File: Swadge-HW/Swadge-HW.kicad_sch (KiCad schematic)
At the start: 178 parts, among them J1 Conn_02x03_Odd_Even, J2 PJ-307C, J3 Conn_01x05_Male, P1 USB_C_Plug_USB2.0, Q1 Q_PMOS_GSD, SW1 YTS-D003-1A, SW2 YTS-D003-1A, SW3 YTS-D003-1A, SW4 YTS-D003-1A, SW5 YTS-D003-1A, SW6 YTS-D003-1A, SW7 B3FS-4002P, SW8 B3FS-4002P, SW9 SW_SPDT_1825232-1, U1 ESP32-S2-MINI-1, U11 CH32V003F4U6, U2 RB017A1505A, U3 M3410, U5 RB017A1505A_Connector, U6 LSM6DSL, U7 GENERIC_LDO_GOI, U8 FM8002A, U9 INGHAi_GSPK2307P-8R1W

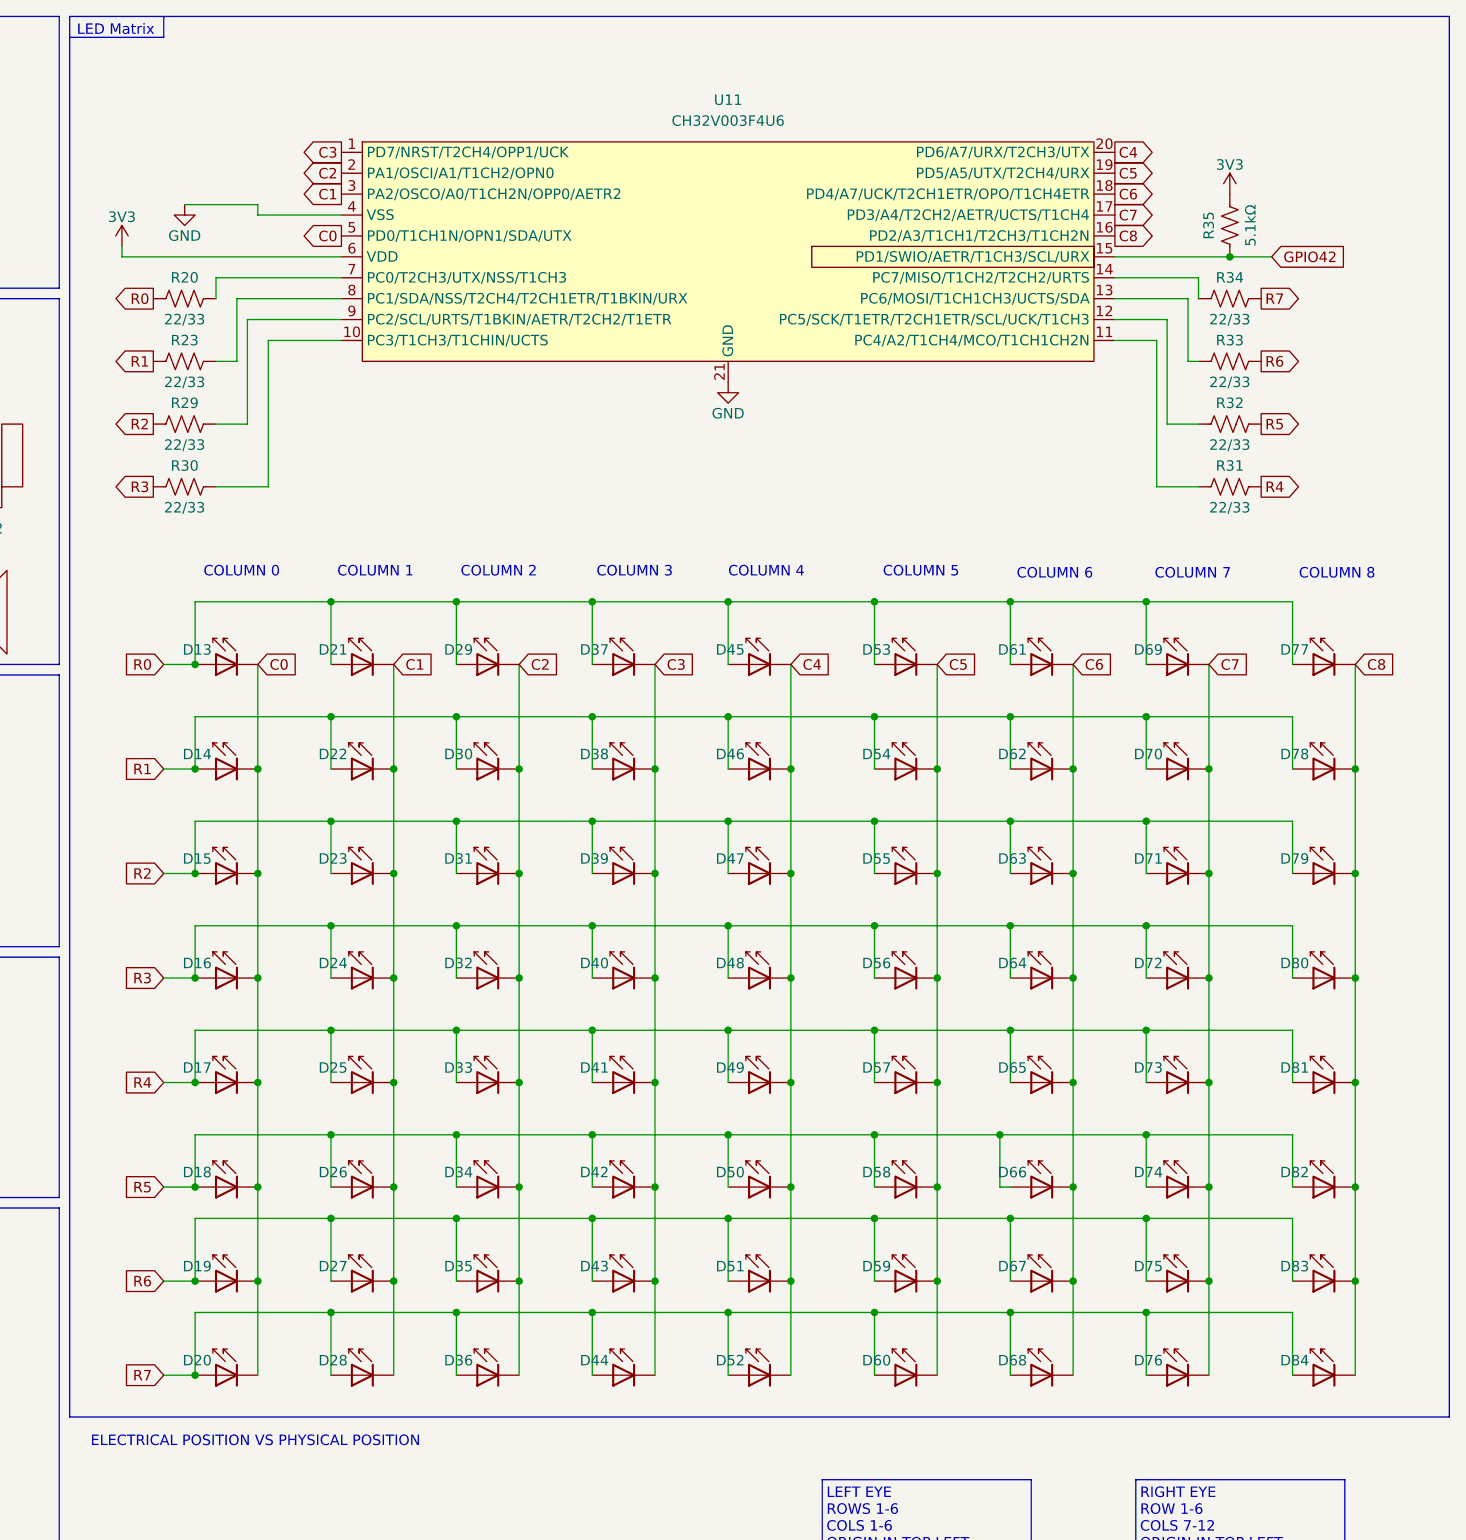
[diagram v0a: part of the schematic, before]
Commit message: DNP the eye LEDs and board outline
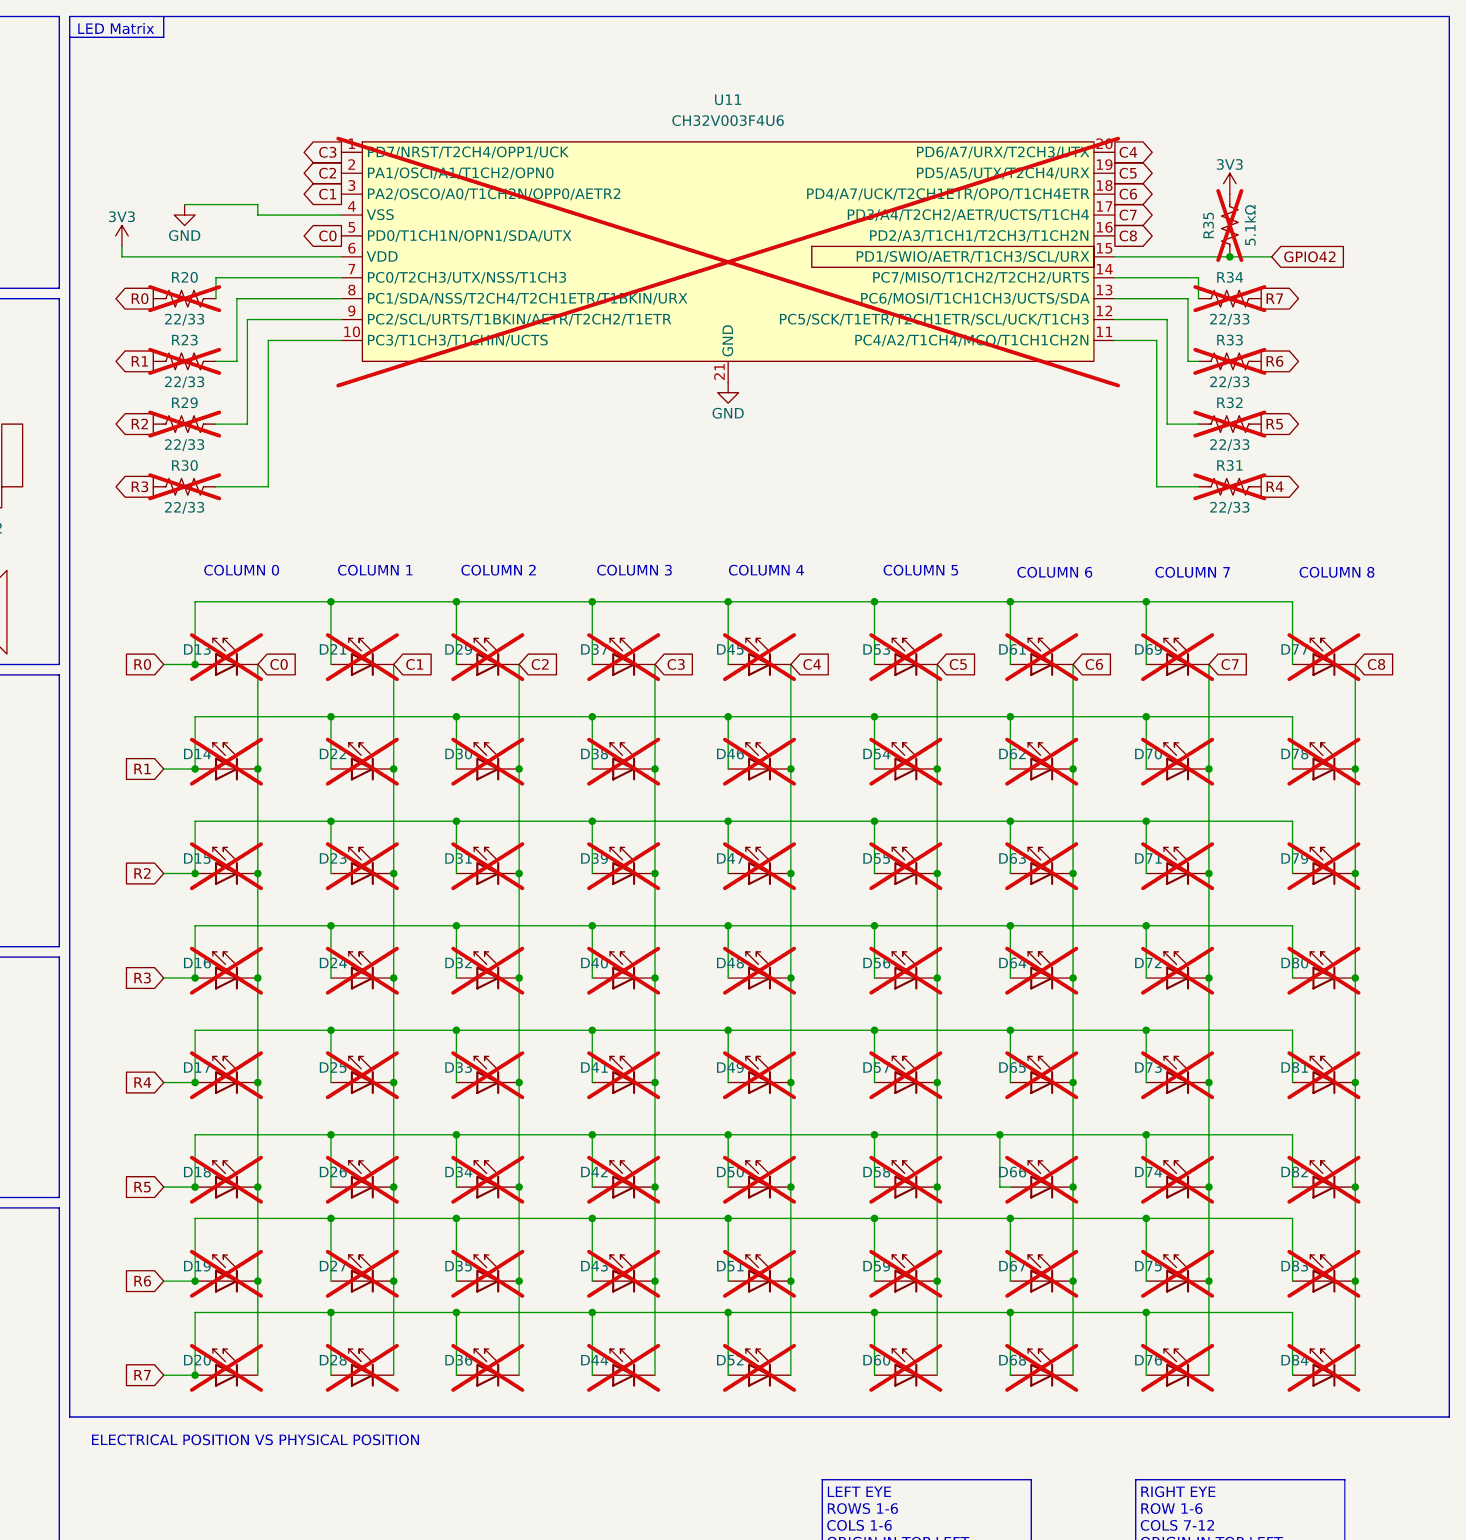
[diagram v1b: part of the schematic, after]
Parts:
- D13, D14, D15, D16, D17, D18, D19, D20, D21, D22, D23, D24, D25, D26, D27, D28, D29, D30, D31, D32, D33, D34, D35, D36, D37, D38, D39, D40, D41, D42, D43, D44, D45, D46, D47, D48, D49, D50, D51, D52, D53, D54, D55, D56, D57, D58, D59, D60, D61, D62, D63, D64, D65, D66, D67, D68, D69, D70, D71, D72, D73, D74, D75, D76, D77, D78, D79, D80, D81, D82, D83, D84, R20, R23, R29, R30, R31, R32, R33, R34, R35, U11: now not fitted; now left out of the parts list

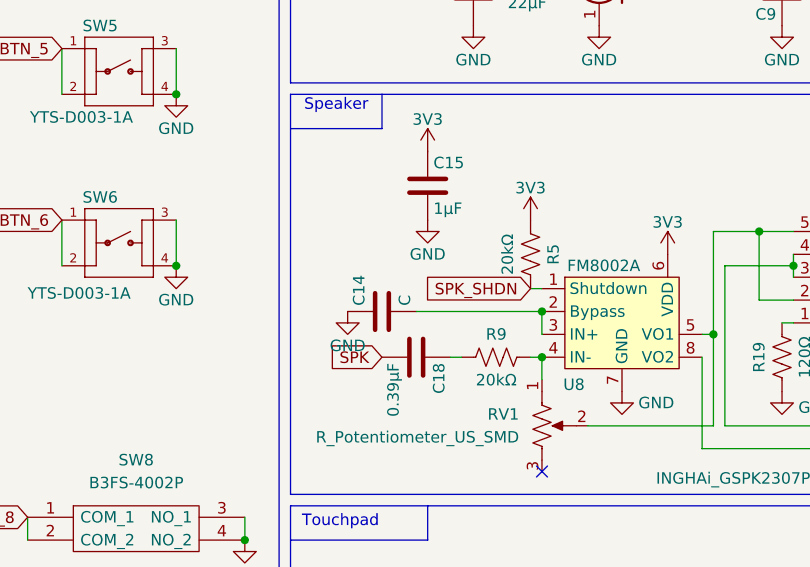
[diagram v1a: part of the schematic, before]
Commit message: Fix LCSC parts
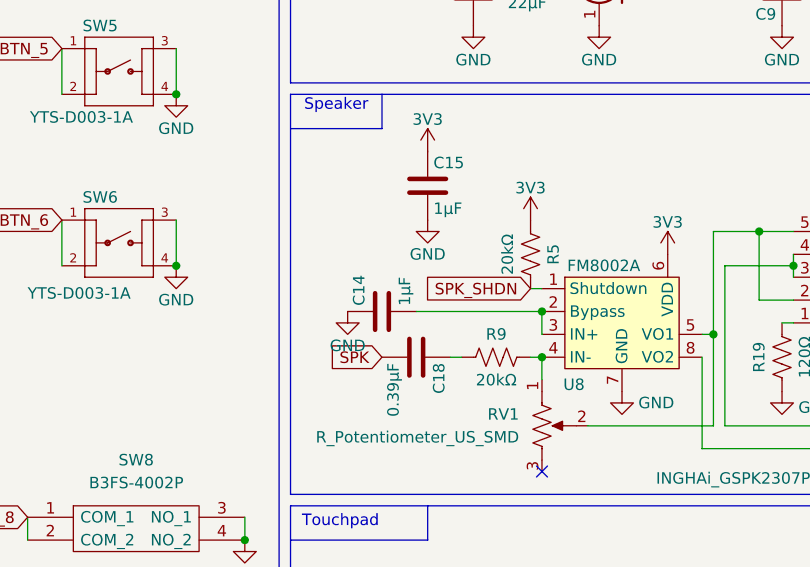
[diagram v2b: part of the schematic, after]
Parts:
- C14: value C -> 1μF
- C7: LCSC C159801 -> C15849

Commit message: Exclude parts from BOM
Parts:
- U2, U4: now left out of the parts list
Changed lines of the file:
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@@
 		(unit 1)
 		(exclude_from_sim no)
-		(in_bom yes)
+		(in_bom no)
 		(on_board yes)
 		(dnp no)
@@
 		(unit 1)
 		(exclude_from_sim no)
-		(in_bom yes)
+		(in_bom no)
 		(on_board yes)
 		(dnp yes)

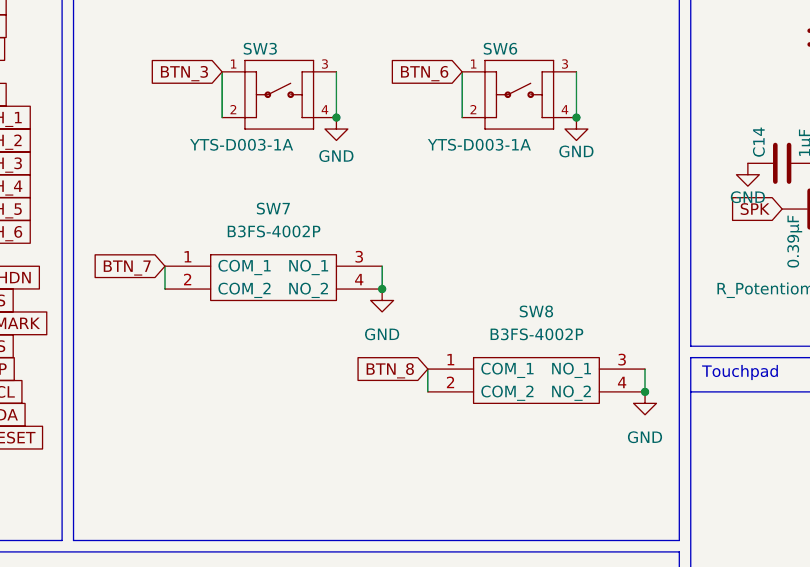
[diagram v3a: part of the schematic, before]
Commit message: Replace tactile switch
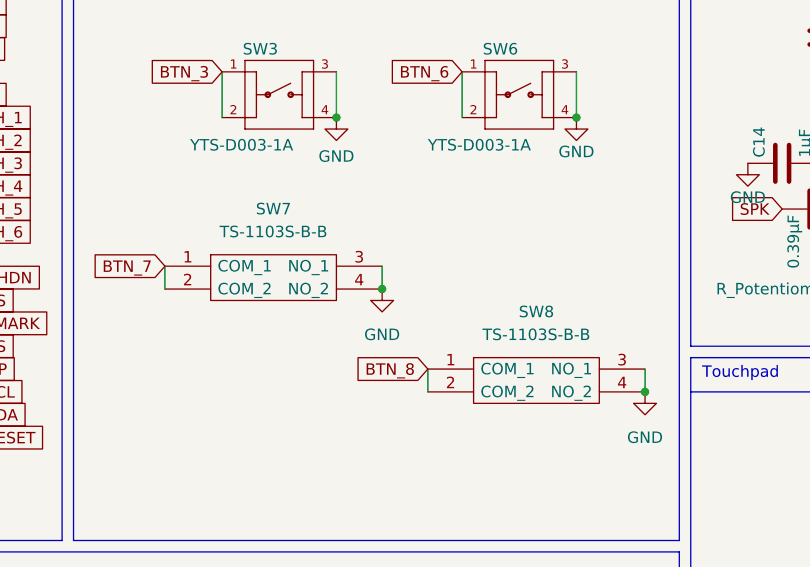
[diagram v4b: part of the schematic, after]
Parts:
- SW7, SW8: value B3FS-4002P -> TS-1103S-B-B; symbol Swadge_Parts:B3FS-4002P -> Swadge_Parts:TS-1103S-B-B; Cost @ 2.5k 0.0461 -> (none); Cost100 76 -> (none); Cost@2500 (none) -> 0.0393; LCSC C5377634 -> C561251
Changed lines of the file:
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@@
 	)
 	(symbol
-		(lib_id "Swadge_Parts:B3FS-4002P")
+		(lib_id "Swadge_Parts:TS-1103S-B-B")
 		(at 146.05 93.98 0)
 		(unit 1)
@@
 			)
 		)
-		(property "Value" "B3FS-4002P"
+		(property "Value" "TS-1103S-B-B"
 			(at 158.115 90.17 0)
 			(effects
@@
 			)
 		)
-		(property "Datasheet" "https://datasheet.lcsc.com/lcsc/1912111437_XUNPU-TS-1003S-04526_C455218.pdf"
+		(property "Datasheet" "https://www.lcsc.com/datasheet/C561251.pdf"
 			(at 166.37 93.98 0)
 			(effects
@@
 			)
 		)
-		(property "Cost100" "76"
-			(at 153.67 82.55 0)
-			(effects
-				(font
-					(size 1.27 1.27)
-				)
-				(hide yes)
-			)
-		)
 		(property "Substitutable" "Y"
 			(at 149.86 81.28 0)
@@
 			)
 		)
-		(property "LCSC" "C5377634"
+		(property "LCSC" "C561251"
 			(at 146.05 93.98 0)
 			(effects
@@
 			)
 		)
-		(property "Cost @ 2.5k" "0.0461"
+		(property "Cost@2500" "0.0393"
 			(at 146.05 93.98 0)
 			(effects
 				(font
-					(size 1.27 1.27)
-				)
-				(hide yes)
-			)
-		)
-		(property "Cost@2500" ""
-			(at 146.05 93.98 0)
-			(effects
-				(font
-					(size 1.27 1.27)
+					(size 1 1)
 				)
 				(hide yes)
@@
 	)
 	(symbol
-		(lib_id "Swadge_Parts:B3FS-4002P")
+		(lib_id "Swadge_Parts:TS-1103S-B-B")
 		(at 116.84 82.55 0)
 		(unit 1)
@@
 			)
 		)
-		(property "Value" "B3FS-4002P"
+		(property "Value" "TS-1103S-B-B"
 			(at 128.905 78.74 0)
 			(effects
@@
 			)
 		)
-		(property "Datasheet" "https://datasheet.lcsc.com/lcsc/1912111437_XUNPU-TS-1003S-04526_C455218.pdf"
+		(property "Datasheet" "https://www.lcsc.com/datasheet/C561251.pdf"
 			(at 137.16 82.55 0)
 			(effects
@@
 			)
 		)
-		(property "Cost100" "76"
-			(at 124.46 71.12 0)
-			(effects
-				(font
-					(size 1.27 1.27)
-				)
-				(hide yes)
-			)
-		)
 		(property "Substitutable" "Y"
 			(at 120.65 69.85 0)
@@
 			)
 		)
-		(property "LCSC" "C5377634"
+		(property "LCSC" "C561251"
 			(at 116.84 82.55 0)
 			(effects
@@
 			)
 		)
-		(property "Cost @ 2.5k" "0.0461"
+		(property "Cost@2500" "0.0393"
 			(at 116.84 82.55 0)
 			(effects
 				(font
-					(size 1.27 1.27)
-				)
-				(hide yes)
-			)
-		)
-		(property "Cost@2500" ""
-			(at 116.84 82.55 0)
-			(effects
-				(font
-					(size 1.27 1.27)
+					(size 1 1)
 				)
 				(hide yes)

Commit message: Replace SAO pins with socket
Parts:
- J1: footprint Swadge_Parts:PinHeader_2x03_P2.54mm_Vertical -> Swadge_Parts:PinSocket_2x03_P2.54mm_Vertical
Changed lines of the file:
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@@
 			)
 		)
-		(property "Footprint" "Swadge_Parts:PinHeader_2x03_P2.54mm_Vertical"
+		(property "Footprint" "Swadge_Parts:PinSocket_2x03_P2.54mm_Vertical"
 			(at 198.12 135.89 0)
 			(effects

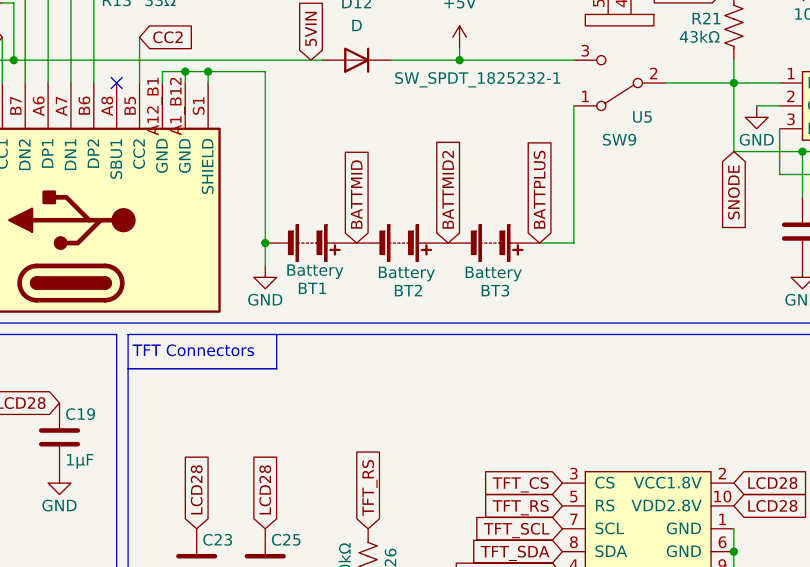
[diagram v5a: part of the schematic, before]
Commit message: Exclude J3 from BOM, Add LCSC for AA holders
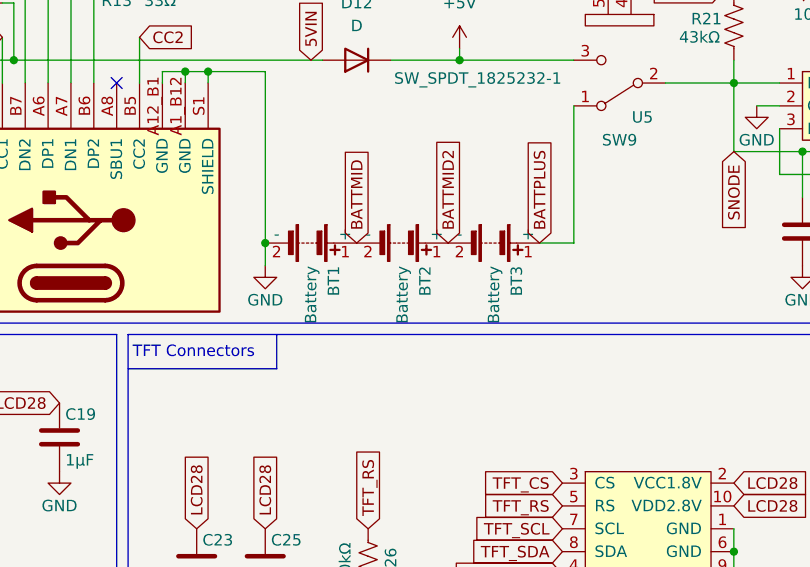
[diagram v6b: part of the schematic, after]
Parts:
- BT1, BT2, BT3: Cost @ 2.5k 0.11 -> 0.9266; Cost100 116 -> (none); LCSC (none) -> C5370863
- J3: now left out of the parts list
- SW7, SW8: Cost @ 2.5k (none) -> 0.0393; Cost@2500 0.0393 -> (none)
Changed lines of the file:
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@@
 		(dnp no)
 		(property "Reference" "BT3"
-			(at 106.426 199.644 90)
+			(at 110.49 196.85 0)
 			(effects
 				(font
@@
 		)
 		(property "Value" "Battery"
-			(at 104.648 197.612 90)
+			(at 107.95 196.85 0)
 			(effects
 				(font
@@
 			)
 		)
-		(property "Cost100" "116"
-			(at 115.57 201.93 0)
-			(effects
-				(font
-					(size 1.27 1.27)
-				)
-				(hide yes)
-			)
-		)
 		(property "Substitutable" "Y"
 			(at 118.11 204.47 0)
@@
 			)
 		)
-		(property "LCSC" "~"
+		(property "LCSC" "C5370863"
 			(at 107.95 194.31 0)
 			(effects
@@
 			)
 		)
-		(property "Cost @ 2.5k" "0.11"
+		(property "Cost @ 2.5k" "0.9266"
 			(at 107.95 194.31 0)
 			(effects
@@
 			)
 		)
-		(property "Cost@2500" ""
-			(at 107.95 194.31 90)
-			(effects
-				(font
-					(size 1.27 1.27)
-				)
-				(hide yes)
-			)
-		)
 		(pin "1"
 		)
@@
 		(dnp no)
 		(property "Reference" "BT1"
-			(at 86.106 199.39 90)
+			(at 90.17 196.85 0)
 			(effects
 				(font
@@
 		)
 		(property "Value" "Battery"
-			(at 84.836 197.358 90)
+			(at 87.63 196.85 0)
 			(effects
 				(font
@@
 			)
 		)
-		(property "Cost100" "116"
-			(at 95.25 201.93 0)
-			(effects
-				(font
-					(size 1.27 1.27)
-				)
-				(hide yes)
-			)
-		)
 		(property "Substitutable" "Y"
 			(at 97.79 204.47 0)
@@
 			)
 		)
-		(property "LCSC" "~"
+		(property "LCSC" "C5370863"
 			(at 87.63 194.31 0)
 			(effects
@@
 			)
 		)
-		(property "Cost @ 2.5k" "0.11"
+		(property "Cost @ 2.5k" "0.9266"
 			(at 87.63 194.31 0)
 			(effects
@@
 			)
 		)
-		(property "Cost@2500" ""
-			(at 87.63 194.31 90)
-			(effects
-				(font
-					(size 1.27 1.27)
-				)
-				(hide yes)
-			)
-		)
 		(pin "1"
 		)
@@
 			)
 		)
-		(property "Cost@2500" "0.0393"
+		(property "Cost @ 2.5k" "0.0393"
 			(at 146.05 93.98 0)
 			(effects
@@
 		(unit 1)
 		(exclude_from_sim no)
-		(in_bom yes)
+		(in_bom no)
 		(on_board yes)
 		(dnp yes)
@@
 			)
 		)
-		(property "Cost@2500" "0.0393"
+		(property "Cost @ 2.5k" "0.0393"
 			(at 116.84 82.55 0)
 			(effects
@@
 		(dnp no)
 		(property "Reference" "BT2"
-			(at 96.774 199.644 90)
+			(at 100.33 196.85 0)
 			(effects
 				(font
@@
 		)
 		(property "Value" "Battery"
-			(at 94.996 197.612 90)
+			(at 97.79 196.85 0)
 			(effects
 				(font
@@
 			)
 		)
-		(property "Cost100" "116"
-			(at 105.41 201.93 0)
-			(effects
-				(font
-					(size 1.27 1.27)
-				)
-				(hide yes)
-			)
-		)
 		(property "Substitutable" "Y"
 			(at 107.95 204.47 0)
@@
 			)
 		)
-		(property "LCSC" "~"
+		(property "LCSC" "C5370863"
 			(at 97.79 194.31 0)
 			(effects
@@
 			)
 		)
-		(property "Cost @ 2.5k" "0.11"
+		(property "Cost @ 2.5k" "0.9266"
 			(at 97.79 194.31 0)
 			(effects
 				(font
-					(size 1.27 1.27)
-				)
-				(hide yes)
-			)
-		)
-		(property "Cost@2500" ""
-			(at 97.79 194.31 90)
-			(effects
-				(font

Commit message: Update inductor LCSC
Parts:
- L1: Cost @ 2.5k 0.0545 -> 0.0483; Cost100 11.16 -> (none); LCSC C90317 -> C223226
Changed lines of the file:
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@@
 			)
 		)
-		(property "Datasheet" "~"
+		(property "Datasheet" "https://www.lcsc.com/datasheet/C223226.pdf"
 			(at 43.18 250.19 0)
 			(effects
@@
 			)
 		)
-		(property "LCSC" "C90317"
-			(at 43.18 250.19 90)
-			(effects
-				(font
-					(size 1.27 1.27)
-				)
-				(hide yes)
-			)
-		)
-		(property "Cost100" "11.16"
+		(property "LCSC" "C223226"
 			(at 43.18 250.19 90)
 			(effects
@@
 			)
 		)
-		(property "Cost @ 2.5k" "0.0545"
+		(property "Cost @ 2.5k" "0.0483"
 			(at 43.18 250.19 0)
 			(effects
 				(font
-					(size 1.27 1.27)
-				)
-				(hide yes)
-			)
-		)
-		(property "Cost@2500" ""
-			(at 43.18 250.19 90)
-			(effects
-				(font
